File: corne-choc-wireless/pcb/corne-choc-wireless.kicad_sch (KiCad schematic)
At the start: 90 parts, among them J2 Nice!View, J4 Nice!View, SW1 SW_PUSH, SW10 SW_PUSH, SW11 SW_PUSH, SW12 SW_PUSH, SW13 SW_PUSH, SW14 SW_PUSH, SW15 SW_PUSH, SW16 SW_PUSH, SW17 SW_PUSH, SW18 SW_PUSH, SW19 SW_PUSH, SW2 SW_PUSH, SW20 SW_PUSH, SW21 SW_PUSH, SW22 SW_PUSH, SW23 SW_PUSH, SW24 SW_PUSH, SW25 SW_PUSH, SW26 SW_PUSH, SW27 SW_PUSH, SW29 SW_PUSH, SW3 SW_PUSH, SW30 SW_PUSH, SW31 SW_PUSH, SW32 SW_PUSH, SW33 SW_PUSH, SW34 SW_PUSH, SW35 SW_PUSH, SW36 SW_PUSH, SW37 SW_PUSH, SW38 SW_PUSH, SW39 SW_PUSH, SW4 SW_PUSH, SW40 SW_PUSH, SW41 SW_PUSH, SW42 SW_PUSH, SW5 SW_PUSH, SW6 SW_PUSH, SW8 SW_PUSH, SW9 SW_PUSH, U1 Nice!Nano, U2 Nice!Nano

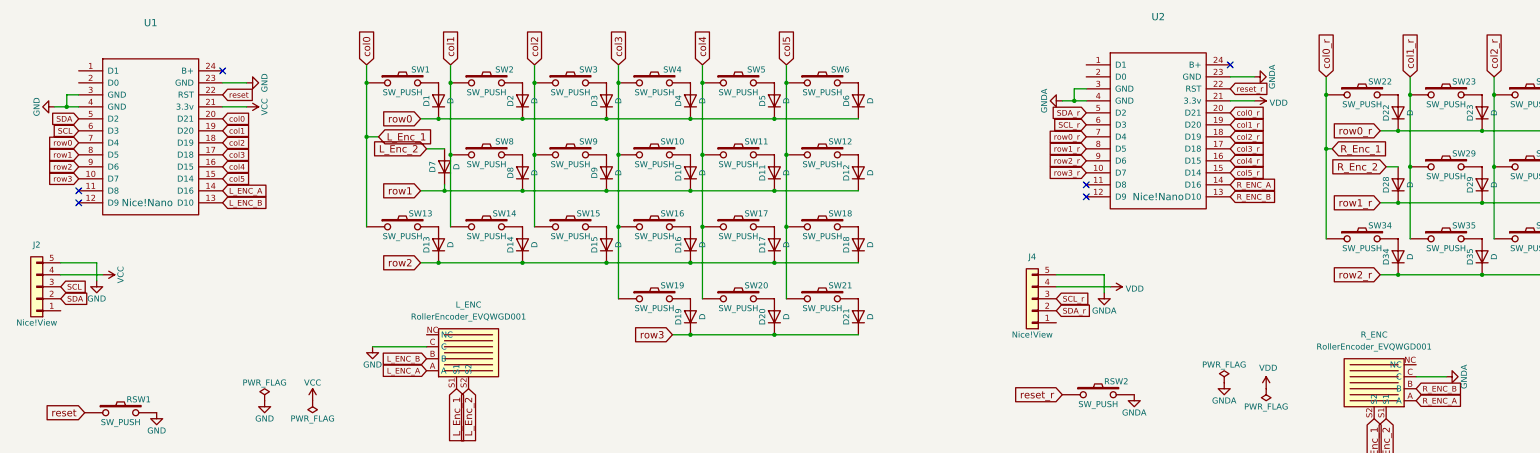
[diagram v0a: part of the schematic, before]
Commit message: Rename and wire up Nice!Views
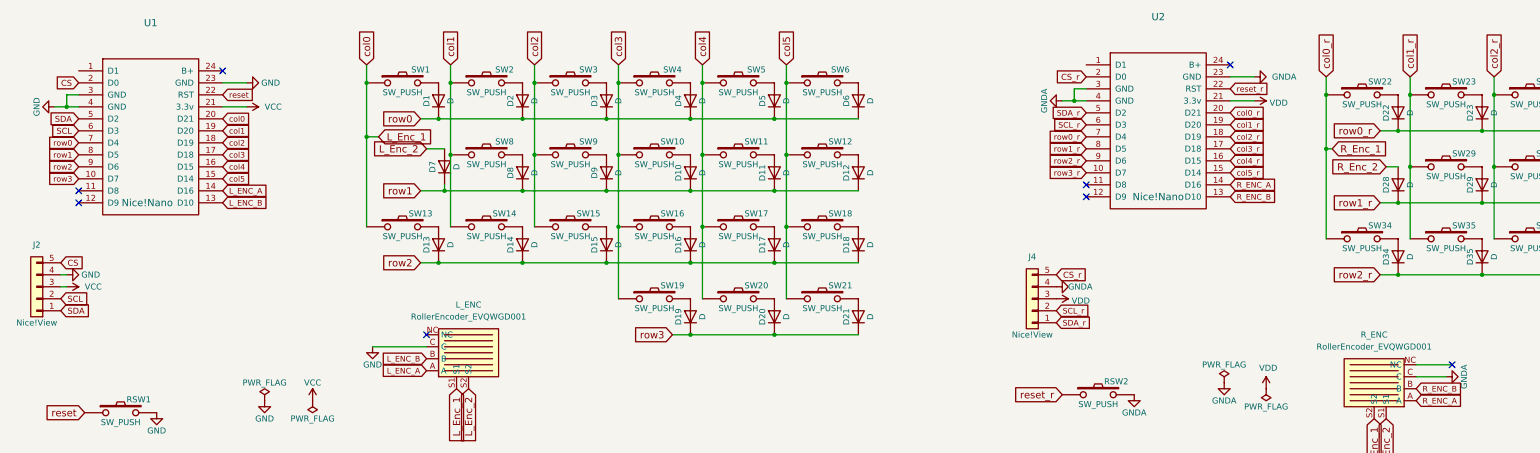
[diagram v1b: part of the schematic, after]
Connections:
- net GND: now also J2.4 (Pin_4); no longer J2.5 (Pin_5)
- net GNDA: now also J4.4 (Pin_4); no longer J4.5 (Pin_5)
- net SCL: now also J2.2 (Pin_2); no longer J2.3 (Pin_3)
- net SCL_r: now also J4.2 (Pin_2); no longer J4.3 (Pin_3)
- net SDA: now also J2.1 (Pin_1); no longer J2.2 (Pin_2)
- net SDA_r: now also J4.1 (Pin_1); no longer J4.2 (Pin_2)
- net VCC: now also J2.3 (Pin_3); no longer J2.4 (Pin_4)
- net VDD: now also J4.3 (Pin_3); no longer J4.4 (Pin_4)
- net CS: now reaches U1.2 (D0)
- net CS: now also J2.5 (Pin_5)
- net CS_r: now reaches U2.2 (D0)
- net CS_r: now also J4.5 (Pin_5)
- no-connect marks 6 -> 8
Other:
- company: foostan -> foostan + GSV-CargoCult
- title: Corne Cherry -> Corne Choc Wireless

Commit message: +BATTA
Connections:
- net +BATT: now reaches U1.24 (B+)
- net +BATTA: now reaches U2.24 (B+)
- no-connect marks 8 -> 6
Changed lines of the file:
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@@
   (no_connect (at 243.84 54.61))
   (no_connect (at 30.48 58.42))
-  (no_connect (at 274.32 29.21))
-  (no_connect (at 60.96 30.48))
   (no_connect (at 104.14 86.36))
   (wire (pts (xy 365.76 50.8) (xy 365.76 66.04))
@@
     (stroke (width 0) (type default))
   )
+  (wire (pts (xy 279.4 29.21) (xy 274.32 29.21))
+    (stroke (width 0) (type default))
+  )
   (wire (pts (xy 321.31 92.71) (xy 313.69 92.71))
     (stroke (width 0) (type default))
@@
     (stroke (width 0) (type default))
   )
+  (wire (pts (xy 66.04 30.48) (xy 60.96 30.48))
+    (stroke (width 0) (type default))
+  )
   (wire (pts (xy 330.2 35.56) (xy 330.2 50.8))
     (stroke (width 0) (type default))
@@
       (effects (font (size 1.27 1.27)) hide)
     )
-    (property "Value" "GND" (at 71.12 33.02 90)
+    (property "Value" "GND" (at 72.39 33.02 90)
       (effects (font (size 1.27 1.27)))
     )
@@
       (effects (font (size 1.27 1.27)) hide)
     )
-    (property "Value" "GNDA" (at 285.75 31.75 90)
+    (property "Value" "GNDA" (at 284.48 31.75 90)
       (effects (font (size 1.27 1.27)))
     )
@@
       (effects (font (size 1.27 1.27)) hide)
     )
-    (property "Value" "VDD" (at 282.6512 37.2618 90)
+    (property "Value" "VDD" (at 281.94 36.83 90)
       (effects (font (size 1.27 1.27)) (justify left))
     )
@@
     )
   )
+  (symbol (lib_id "power:+BATT") (at 59.69 100.33 0) (unit 1)
+    (in_bom yes) (on_board yes) (dnp no)
+    (property "Reference" "#PWR03" (at 59.69 104.14 0)
+      (effects (font (size 1.27 1.27)) hide)
+    )
+    (property "Value" "+BATT" (at 59.69 96.52 0)
+      (effects (font (size 1.27 1.27)))
+    )
+    (property "Footprint" "" (at 59.69 100.33 0)
+      (effects (font (size 1.27 1.27)) hide)
+    )
+    (property "Datasheet" "" (at 59.69 100.33 0)
+      (effects (font (size 1.27 1.27)) hide)
+    )
+    (pin "1")
+    (instances
+      (project "corne-choc-wireless"
+        (path "/745fa137-bada-4eb6-9f49-9b255d7ae8bf"
+          (reference "#PWR03") (unit 1)
+        )
+      )
+    )
+  )
+  (symbol (lib_id "power:+BATTA") (at 262.89 97.79 0) (unit 1)
+    (in_bom yes) (on_board yes) (dnp no) (fields_autoplaced)
+    (property "Reference" "#PWR011" (at 262.89 101.6 0)
+      (effects (font (size 1.27 1.27)) hide)
+    )
+    (property "Value" "+BATTA" (at 262.89 92.71 0)
+      (effects (font (size 1.27 1.27)))
+    )
+    (property "Footprint" "" (at 262.89 97.79 0)
+      (effects (font (size 1.27 1.27)) hide)
+    )
+    (property "Datasheet" "" (at 262.89 97.79 0)
+      (effects (font (size 1.27 1.27)) hide)
+    )
+    (pin "1")
+    (instances
+      (project "corne-choc-wireless"
+        (path "/745fa137-bada-4eb6-9f49-9b255d7ae8bf"
+          (reference "#PWR011") (unit 1)
+        )
+      )
+    )
+  )
   (symbol (lib_id "zzkeebs:RollerEncoder_EVQWGD001") (at 111.76 88.9 0) (mirror x) (unit 1)
     (in_bom yes) (on_board yes) (dnp no)
@@
     )
   )
+  (symbol (lib_id "power:PWR_FLAG") (at 262.89 97.79 180) (unit 1)
+    (in_bom yes) (on_board yes) (dnp no)
+    (property "Reference" "#FLG06" (at 262.89 99.695 0)
+      (effects (font (size 1.27 1.27)) hide)
+    )
+    (property "Value" "PWR_FLAG" (at 262.89 101.6 0)
+      (effects (font (size 1.27 1.27)))
+    )
+    (property "Footprint" "" (at 262.89 97.79 0)
+      (effects (font (size 1.27 1.27)) hide)
+    )
+    (property "Datasheet" "" (at 262.89 97.79 0)
+      (effects (font (size 1.27 1.27)) hide)
+    )
+    (pin "1")
+    (instances
+      (project "corne-choc-wireless"
+        (path "/745fa137-bada-4eb6-9f49-9b255d7ae8bf"
+          (reference "#FLG06") (unit 1)
+        )
+      )
+    )
+  )
+  (symbol (lib_id "power:+BATTA") (at 279.4 29.21 270) (unit 1)
+    (in_bom yes) (on_board yes) (dnp no)
+    (property "Reference" "#PWR012" (at 275.59 29.21 0)
+      (effects (font (size 1.27 1.27)) hide)
+    )
+    (property "Value" "+BATTA" (at 281.94 29.21 90)
+      (effects (font (size 1.27 1.27)) (justify left))
+    )
+    (property "Footprint" "" (at 279.4 29.21 0)
+      (effects (font (size 1.27 1.27)) hide)
+    )
+    (property "Datasheet" "" (at 279.4 29.21 0)
+      (effects (font (size 1.27 1.27)) hide)
+    )
+    (pin "1")
+    (instances
+      (project "corne-choc-wireless"
+        (path "/745fa137-bada-4eb6-9f49-9b255d7ae8bf"
+          (reference "#PWR012") (unit 1)
+        )
+      )
+    )
+  )
   (symbol (lib_id "Device:D") (at 107.95 50.8 90) (unit 1)
     (in_bom yes) (on_board yes) (dnp no)
@@
         )
       )
+    )
+  )
+  (symbol (lib_id "power:PWR_FLAG") (at 59.69 100.33 180) (unit 1)
+    (in_bom yes) (on_board yes) (dnp no)
+    (property "Reference" "#FLG05" (at 59.69 102.235 0)
+      (effects (font (size 1.27 1.27)) hide)
+    )
+    (property "Value" "PWR_FLAG" (at 59.69 104.14 0)
+      (effects (font (size 1.27 1.27)))
+    )
+    (property "Footprint" "" (at 59.69 100.33 0)
+      (effects (font (size 1.27 1.27)) hide)
+    )
+    (property "Datasheet" "" (at 59.69 100.33 0)
+      (effects (font (size 1.27 1.27)) hide)
+    )
+    (pin "1")
+    (instances
+      (project "corne-choc-wireless"
+        (path "/745fa137-bada-4eb6-9f49-9b255d7ae8bf"
+          (reference "#FLG05") (unit 1)
+        )
+      )
+    )
+  )
+  (symbol (lib_id "power:+BATT") (at 66.04 30.48 270) (unit 1)
+    (in_bom yes) (on_board yes) (dnp no) (fields_autoplaced)
+    (property "Reference" "#PWR02" (at 62.23 30.48 0)
+      (effects (font (size 1.27 1.27)) hide)
+    )
+    (property "Value" "+BATT" (at 69.85 30.48 90)
+      (effects (font (size 1.27 1.27)) (justify left))
+    )
+    (property "Footprint" "" (at 66.04 30.48 0)
+      (effects (font (size 1.27 1.27)) hide)
+    )
+    (property "Datasheet" "" (at 66.04 30.48 0)
+      (effects (font (size 1.27 1.27)) hide)
+    )
+    (pin "1")
+    (instances
+      (project "corne-choc-wireless"
+        (path "/745fa137-bada-4eb6-9f49-9b255d7ae8bf"
+          (reference "#PWR02") (unit 1)
+        )
+      )

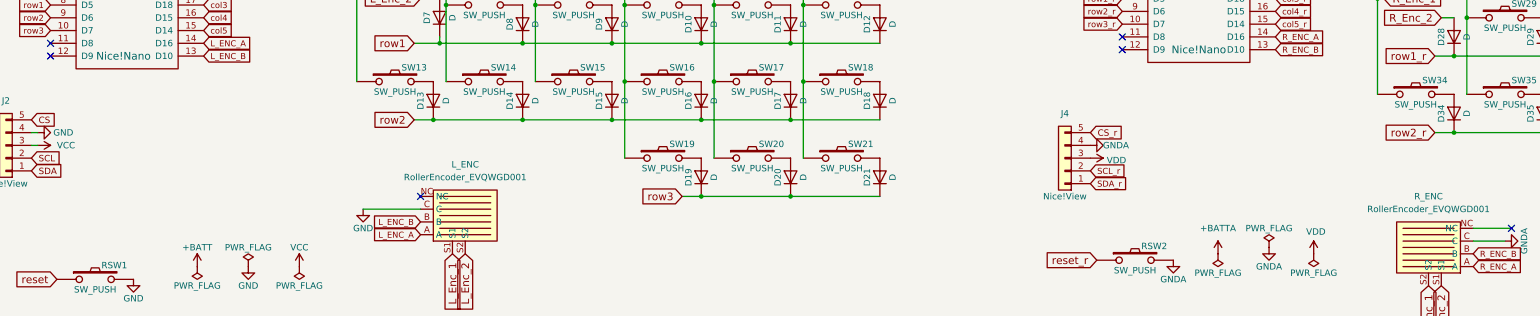
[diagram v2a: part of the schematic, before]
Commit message: Map new footprints
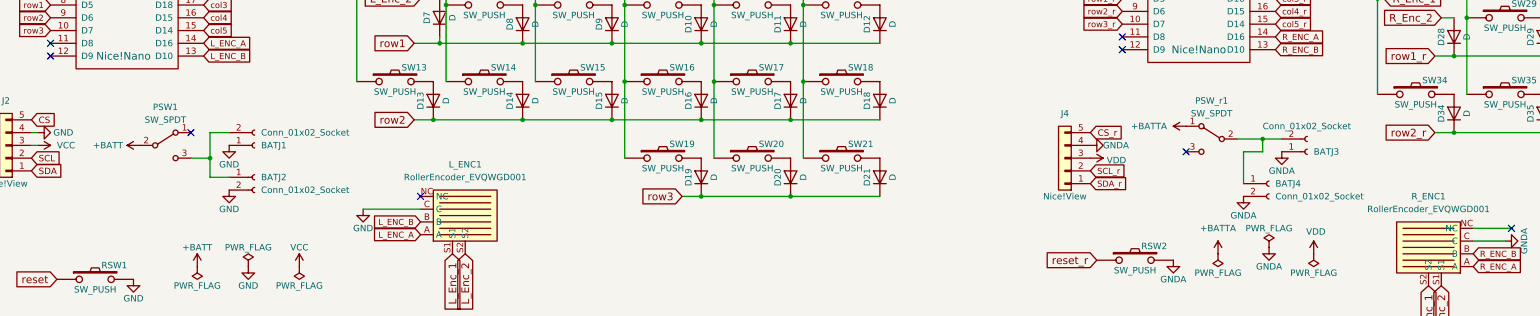
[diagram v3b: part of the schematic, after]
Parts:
- added BATJ1, BATJ3: Conn_01x02_Socket, Connector_PinHeader_2.54mm:PinHeader_1x02_P2.54mm_Vertical, symbol Connector:Conn_01x02_Socket
- added BATJ2, BATJ4: Conn_01x02_Socket, Connector_JST:JST_PH_S2B-PH-K_1x02_P2.00mm_Horizontal, symbol Connector:Conn_01x02_Socket
- added PSW1, PSW_r1: SW_SPDT, Button_Switch_SMD:SW_SPDT_PCM12, symbol Switch:SW_SPDT
- J2, J4: footprint kbd:OLED_1side -> niceview:nice_view_1side
- L_ENC1: renamed from L_ENC; footprint (none) -> zzkeeb:RotaryEncoder_EVQWGD001
- R_ENC1: renamed from R_ENC; footprint (none) -> zzkeeb:RotaryEncoder_EVQWGD001
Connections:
- net +BATT: now also PSW1.2 (B)
- net +BATTA: now also PSW_r1.1 (A)
- net GND: now also BATJ1.1 (Pin_1), BATJ2.2 (Pin_2)
- net GNDA: now also BATJ3.1 (Pin_1), BATJ4.2 (Pin_2)
- new net: BATJ1.2 (Pin_2), BATJ2.1 (Pin_1), PSW1.3 (C)
- new net: BATJ3.2 (Pin_2), BATJ4.1 (Pin_1), PSW_r1.2 (B)
- no-connect marks 6 -> 8

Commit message: Fix edge cuts
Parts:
- U1, U2: footprint ScottoKeebs_MCU:Nice_Nano_V2 -> kbd:ProMicro_v3
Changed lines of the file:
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@@
       (effects (font (size 1.524 1.524)))
     )
-    (property "Footprint" "ScottoKeebs_MCU:Nice_Nano_V2" (at 45.72 67.31 0)
+    (property "Footprint" "kbd:ProMicro_v3" (at 45.72 67.31 0)
       (effects (font (size 1.524 1.524)) hide)
     )
@@
       (effects (font (size 1.524 1.524)))
     )
-    (property "Footprint" "ScottoKeebs_MCU:Nice_Nano_V2" (at 259.08 66.04 0)
+    (property "Footprint" "kbd:ProMicro_v3" (at 259.08 66.04 0)
       (effects (font (size 1.524 1.524)) hide)
     )

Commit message: All traces done
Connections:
- net R_ENC_A: now also U2.12 (D9); no longer U2.14 (D16)
- net R_ENC_B: now also U2.11 (D8); no longer U2.13 (D10)
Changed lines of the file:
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@@
   )
   (no_connect (at 321.31 92.71))
-  (no_connect (at 243.84 57.15))
   (no_connect (at 30.48 55.88))
-  (no_connect (at 243.84 54.61))
+  (no_connect (at 274.32 54.61))
   (no_connect (at 256.54 77.47))
   (no_connect (at 30.48 58.42))
+  (no_connect (at 274.32 57.15))
   (no_connect (at 58.42 73.66))
   (no_connect (at 104.14 86.36))
@@
   )
   (wire (pts (xy 241.3 36.83) (xy 243.84 36.83))
+    (stroke (width 0) (type default))
+  )
+  (wire (pts (xy 240.03 57.15) (xy 243.84 57.15))
     (stroke (width 0) (type default))
   )
@@
     )
   )
-  (global_label "R_ENC_B" (shape input) (at 274.32 57.15 0)
-    (effects (font (size 1.1938 1.1938)) (justify left))
-    (property "Intersheetrefs" "${INTERSHEET_REFS}" (at 274.32 57.15 0)
-      (effects (font (size 1.27 1.27)) hide)
-    )
-  )
   (global_label "SCL" (shape input) (at 26.67 78.74 0) (fields_autoplaced)
     (effects (font (size 1.27 1.27)) (justify left))
@@
     )
   )
+  (global_label "R_ENC_B" (shape input) (at 243.84 54.61 180)
+    (effects (font (size 1.1938 1.1938)) (justify right))
+    (property "Intersheetrefs" "${INTERSHEET_REFS}" (at 243.84 54.61 0)
+      (effects (font (size 1.27 1.27)) hide)
+    )
+  )
   (global_label "CS_r" (shape input) (at 237.49 73.66 0) (fields_autoplaced)
     (effects (font (size 1.27 1.27)) (justify left))
@@
     )
   )
-  (global_label "R_ENC_A" (shape input) (at 274.32 54.61 0)
-    (effects (font (size 1.1938 1.1938)) (justify left))
-    (property "Intersheetrefs" "${INTERSHEET_REFS}" (at 274.32 54.61 0)
-      (effects (font (size 1.27 1.27)) hide)
-    )
+  (global_label "R_ENC_A" (shape input) (at 243.84 57.15 180)
+    (effects (font (size 1.1938 1.1938)) (justify right))
+    (property "Intersheetrefs" "${INTERSHEET_REFS}" (at 243.84 57.15 0)
+      (effects (font (size 1.27 1.27)) hide)
+    )

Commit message: Choc Done YAY
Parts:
- SW1, SW10, SW11, SW12, SW13, SW14, SW15, SW16, SW17, SW18, SW19, SW2, SW20, SW22, SW23, SW24, SW25, SW26, SW27, SW29, SW3, SW30, SW31, SW32, SW33, SW34, SW35, SW36, SW37, SW38, SW39, SW4, SW40, SW41, SW5, SW6, SW8, SW9: footprint kbd:CherryMX_Hotswap -> Library:Hotswap_Choc_V1_MX_1.00u
- SW21, SW42: footprint kbd:CherryMX_Hotswap_1.5u -> ScottoKeebs_Hotswap:Hotswap_Choc_V1_1.50u
